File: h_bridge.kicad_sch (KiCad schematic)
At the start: 8 parts, among them Q3 FDMT80080DC, Q4 FDMT80080DC, X2 Conn_01x01

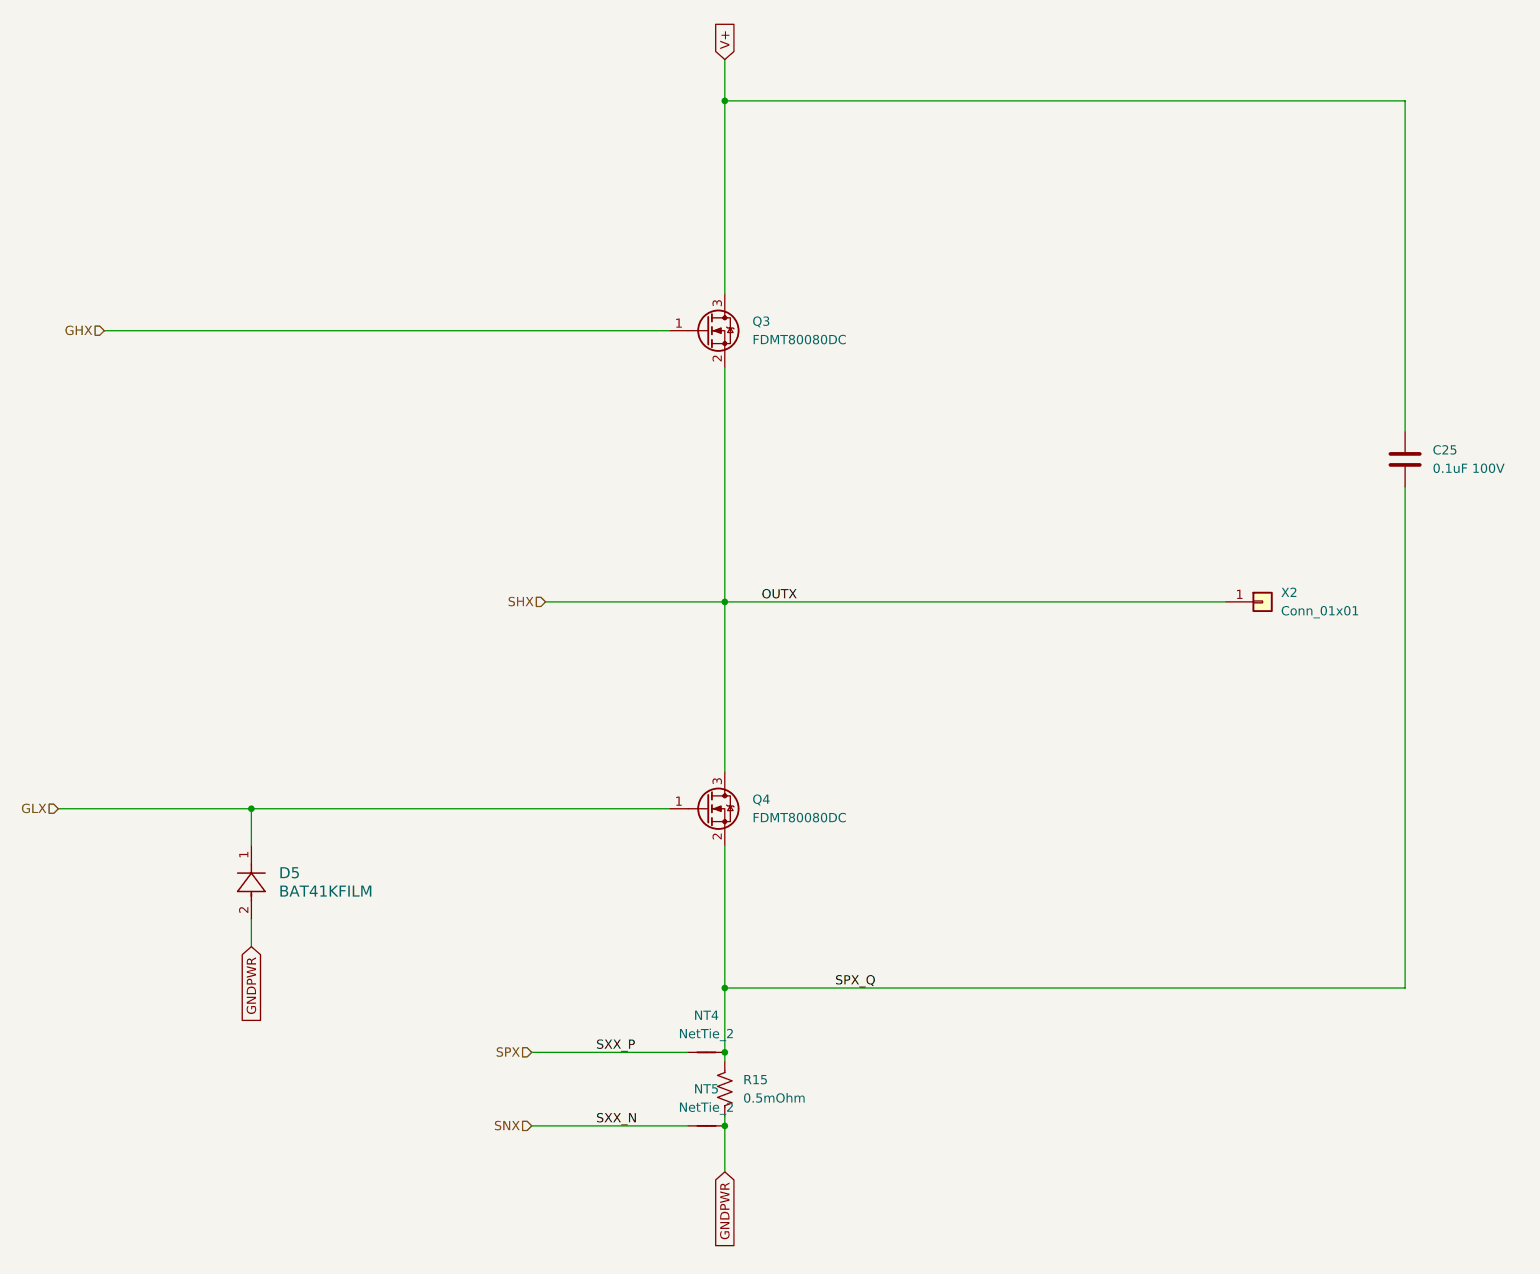
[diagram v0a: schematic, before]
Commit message: MCU sheet edits: move VBUS to PA2, add USART3 on PE15/PB10
Schematic files re-saved in KiCad 10 format. Ignore VS Code .history/.

Co-Authored-By: Claude Opus 5.5 <noreply@anthropic.com>
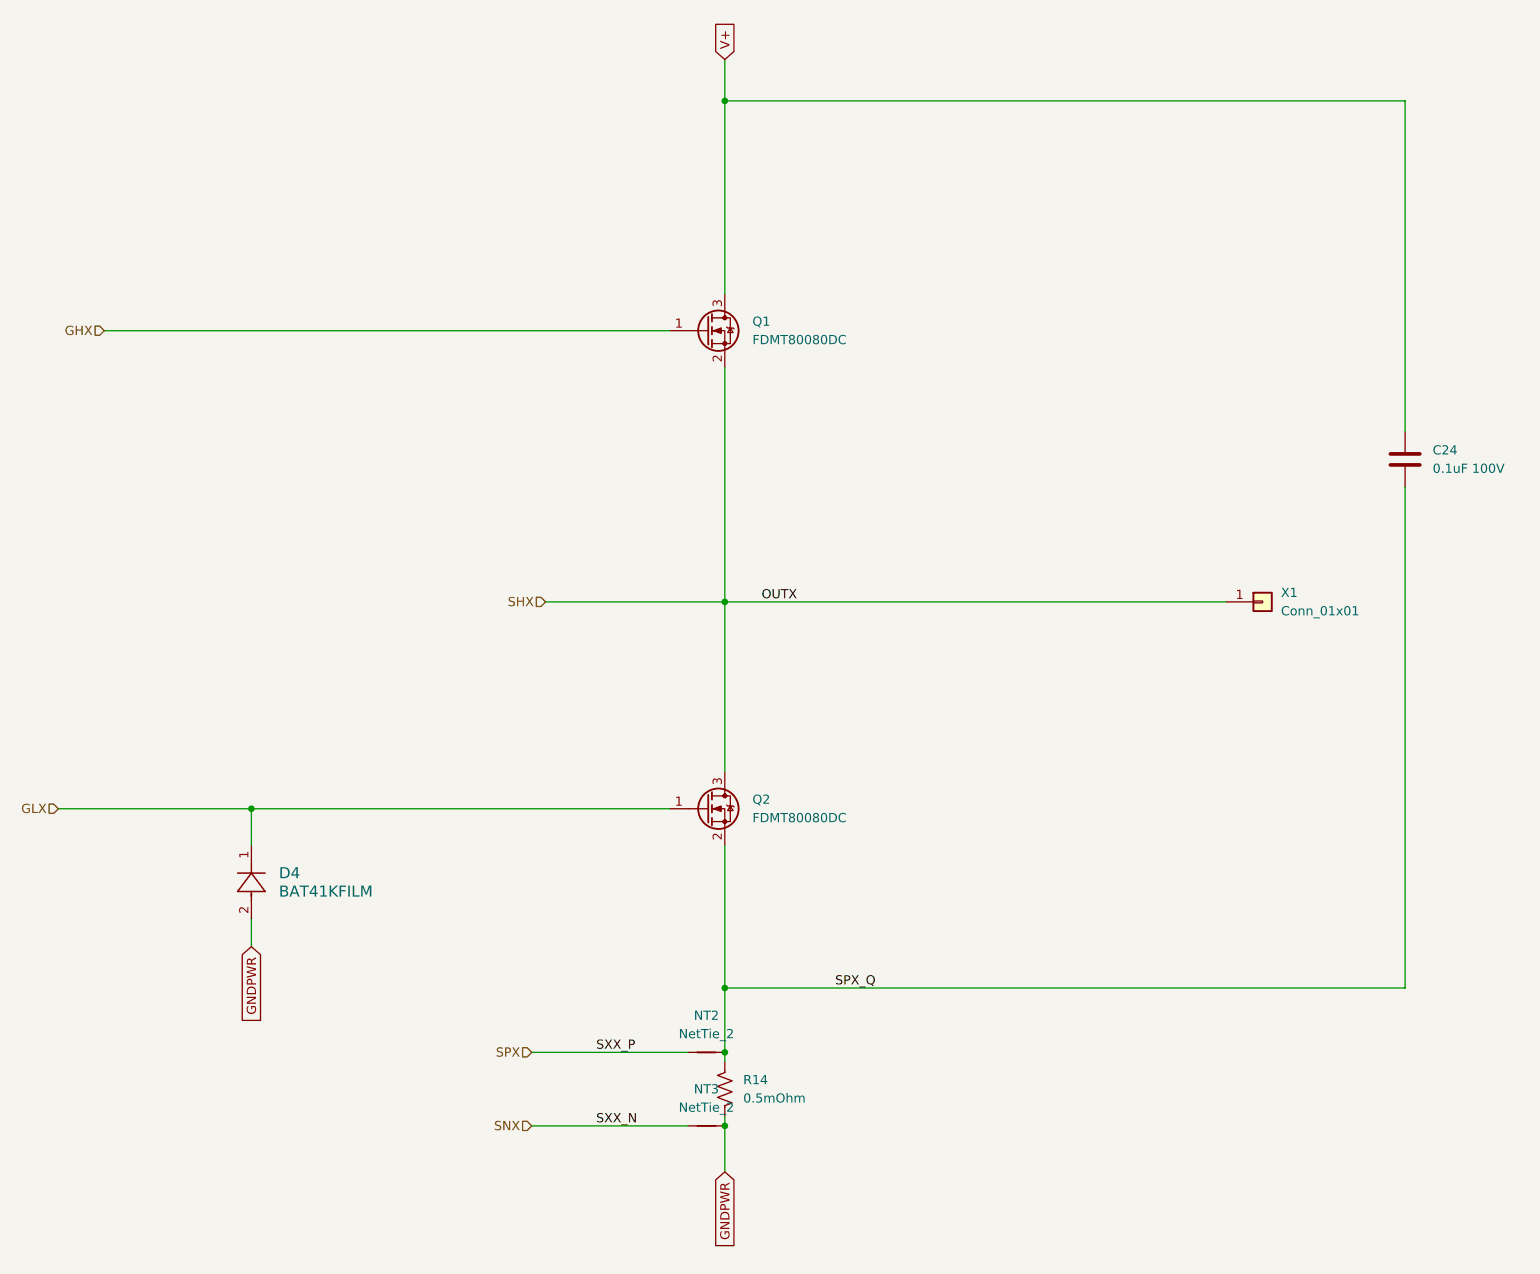
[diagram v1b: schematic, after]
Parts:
- renumbered C25 to C24, D5 to D4, NT4 to NT2, NT5 to NT3, Q3 to Q1, Q4 to Q2, R15 to R14, X2 to X1
